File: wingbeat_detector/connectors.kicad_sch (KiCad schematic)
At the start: 2 parts, among them J1 USB_C_10137062-00021LF, J2 CONN_UMC_JACK_SMD

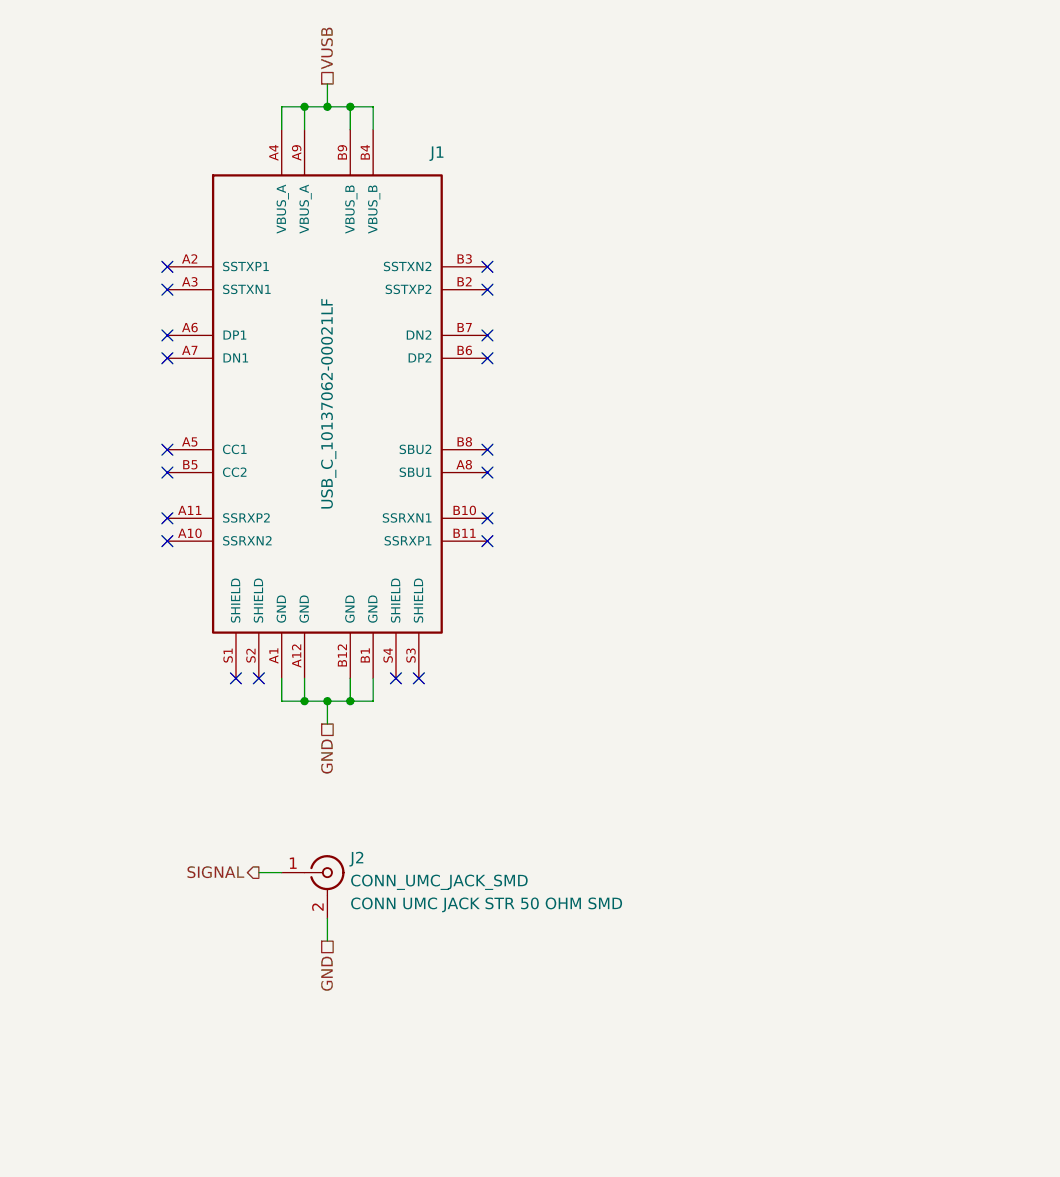
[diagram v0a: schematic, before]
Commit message: Add led driver
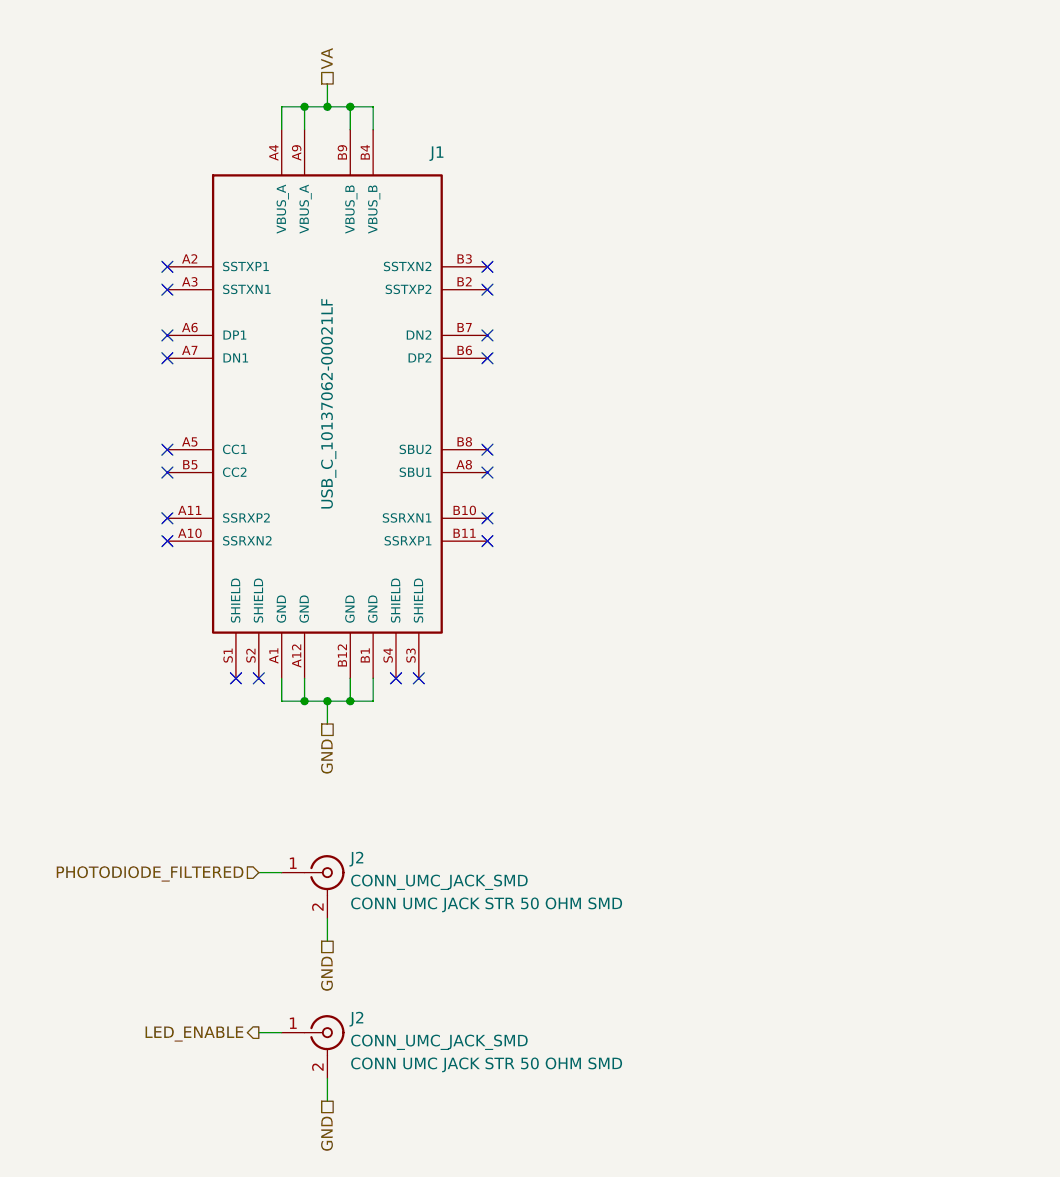
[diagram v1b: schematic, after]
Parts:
- added J2: CONN_UMC_JACK_SMD, Janelia:UMC_AMPHENOL_A-1JB, symbol Janelia:CONN_UMC_JACK_SMD
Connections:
- net GND: now also J2.2 (Ext)
- net SIGNAL renamed PHOTODIODE_FILTERED
- net VUSB renamed VA
- new net LED_ENABLE: J2.1 (In)
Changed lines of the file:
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@@
+    (stroke (width 0) (type default))
+  )
+  (wire (pts (xy 156.21 147.32) (xy 158.75 147.32))
     (stroke (width 0) (type default))
   )
@@
     (stroke (width 0) (type default))
   )
+  (wire (pts (xy 163.83 152.4) (xy 163.83 154.94))
+    (stroke (width 0) (type default))
+  )
   (wire (pts (xy 161.29 44.45) (xy 161.29 46.99))
     (stroke (width 0) (type default))
   )
-  (hierarchical_label "VUSB" (shape passive) (at 163.83 41.91 90) (fields_autoplaced)
+  (hierarchical_label "VA" (shape passive) (at 163.83 41.91 90) (fields_autoplaced)
     (effects (font (size 1.27 1.27)) (justify left))
   )
@@
     (effects (font (size 1.27 1.27)) (justify right))
   )
-  (hierarchical_label "SIGNAL" (shape output) (at 156.21 129.54 180) (fields_autoplaced)
+  (hierarchical_label "PHOTODIODE_FILTERED" (shape input) (at 156.21 129.54 180) (fields_autoplaced)
     (effects (font (size 1.27 1.27)) (justify right))
   )
+  (hierarchical_label "GND" (shape passive) (at 163.83 154.94 270) (fields_autoplaced)
+    (effects (font (size 1.27 1.27)) (justify right))
+  )
+  (hierarchical_label "LED_ENABLE" (shape output) (at 156.21 147.32 180) (fields_autoplaced)
+    (effects (font (size 1.27 1.27)) (justify right))
+  )
+  (symbol (lib_id "Janelia:CONN_UMC_JACK_SMD") (at 163.83 147.32 0) (unit 1)
+    (in_bom yes) (on_board yes) (dnp no) (fields_autoplaced)
+    (property "Reference" "J2" (at 166.37 145.7082 0)
+      (effects (font (size 1.27 1.27)) (justify left))
+    )
+    (property "Value" "CONN_UMC_JACK_SMD" (at 166.37 148.2482 0)
+      (effects (font (size 1.27 1.27)) (justify left))
+    )
+    (property "Footprint" "Janelia:UMC_AMPHENOL_A-1JB" (at 163.83 147.32 0)
+      (effects (font (size 1.27 1.27)) hide)
+    )
+    (property "Datasheet" "" (at 163.83 147.32 0)
+      (effects (font (size 1.27 1.27)) hide)
+    )
+    (property "Manufacturer" "Amphenol RF" (at 163.83 147.32 0)
+      (effects (font (size 1.27 1.27)) hide)
+    )
+    (property "Manufacturer Part Number" "A-1JB" (at 163.83 147.32 0)
+      (effects (font (size 1.27 1.27)) hide)
+    )
+    (property "Vendor" "Digi-Key" (at 163.83 147.32 0)
+      (effects (font (size 1.27 1.27)) hide)
+    )
+    (property "Vendor Part Number" "115-A-1JBCT-ND" (at 163.83 147.32 0)
+      (effects (font (size 1.27 1.27)) hide)
+    )
+    (property "Description" "CONN UMC JACK STR 50 OHM SMD" (at 166.37 150.7882 0)
+      (effects (font (size 1.27 1.27)) (justify left))
+    )
+    (pin "1")
+    (pin "2")
+    (instances
+      (project "wingbeat_detector"
+        (path "/cc457ebc-4af6-4663-b19f-8cb38f061cb4"
+          (reference "J2") (unit 1)
+        )
+        (path "/cc457ebc-4af6-4663-b19f-8cb38f061cb4/6cde90e6-6156-42e3-aaac-c45ad2bfab8b"
+          (reference "J2") (unit 1)
+        )
+        (path "/cc457ebc-4af6-4663-b19f-8cb38f061cb4/f56db15f-9297-4fc0-bdbb-85a25a2944ba"
+          (reference "J3") (unit 1)
+        )
+      )
+    )
+  )
   (symbol (lib_id "Janelia:CONN_UMC_JACK_SMD") (at 163.83 129.54 0) (unit 1)

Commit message: Add mosfet and opa381
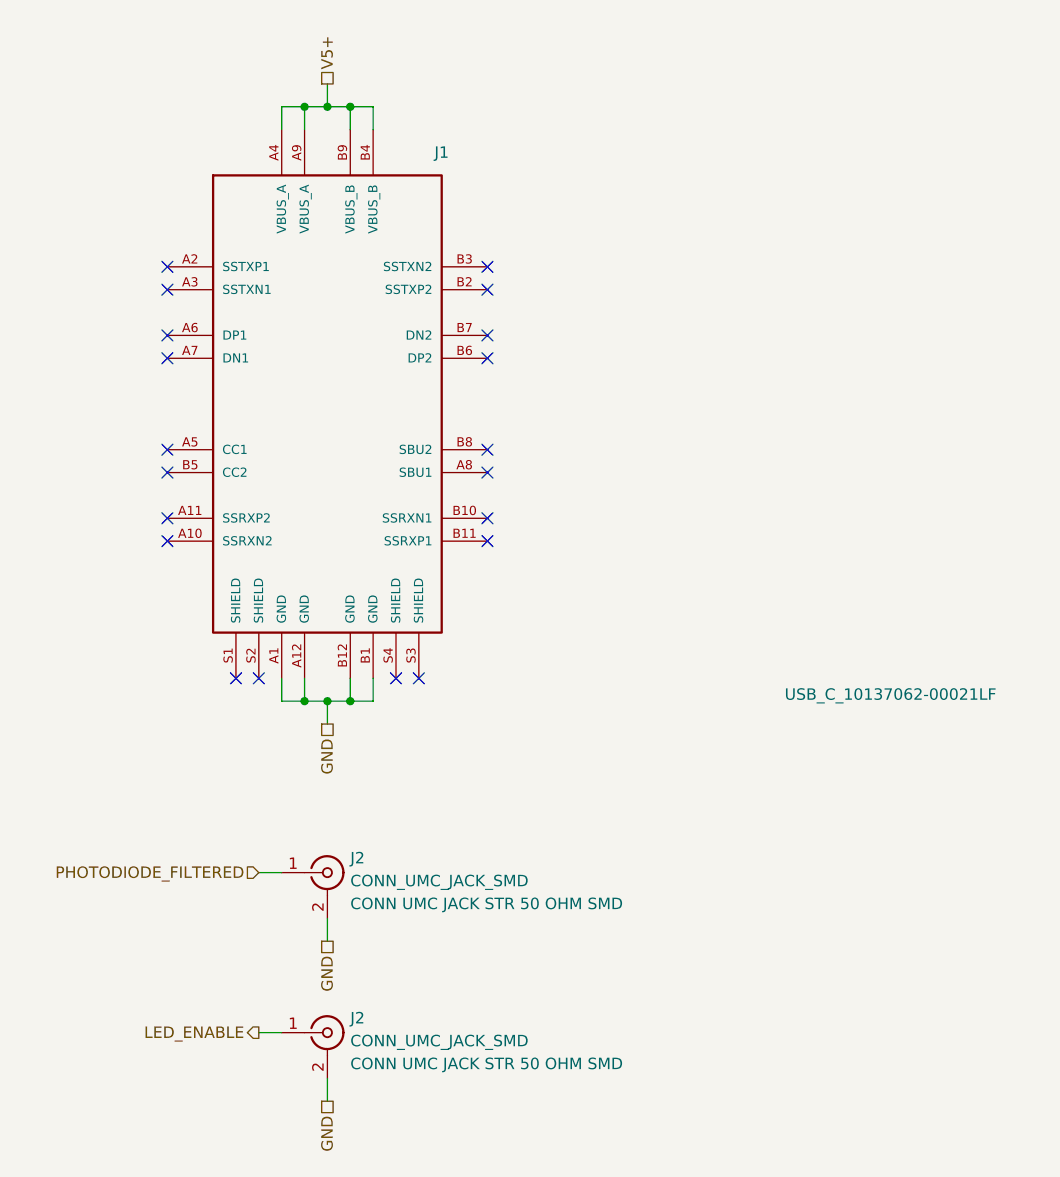
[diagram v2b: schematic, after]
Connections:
- net VA renamed V5+
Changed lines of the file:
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@@
     (stroke (width 0) (type default))
   )
-  (hierarchical_label "VA" (shape passive) (at 163.83 41.91 90) (fields_autoplaced)
+  (hierarchical_label "V5+" (shape passive) (at 163.83 41.91 90) (fields_autoplaced)
     (effects (font (size 1.27 1.27)) (justify left))
   )
@@
         )
         (path "/cc457ebc-4af6-4663-b19f-8cb38f061cb4/f56db15f-9297-4fc0-bdbb-85a25a2944ba"
-          (reference "J3") (unit 1)
+          (reference "J?") (unit 1)
         )
       )
@@
         )
         (path "/cc457ebc-4af6-4663-b19f-8cb38f061cb4/f56db15f-9297-4fc0-bdbb-85a25a2944ba"
-          (reference "J2") (unit 1)
+          (reference "J?") (unit 1)
         )
       )
@@
   (symbol (lib_id "Janelia:USB_C_10137062-00021LF") (at 163.83 77.47 0) (unit 1)
     (in_bom yes) (on_board yes) (dnp no)
-    (property "Reference" "J1" (at 175.26 49.53 0)
-      (effects (font (size 1.27 1.27)) (justify left))
-    )
-    (property "Value" "USB_C_10137062-00021LF" (at 163.83 77.47 90)
+    (property "Reference" "J1" (at 176.53 49.53 0)
       (effects (font (size 1.27 1.27)))
     )
-    (property "Footprint" "Janelia:USB_C_Receptacle_Amphenol_10137062-00021LF" (at 163.83 77.47 0)
+    (property "Value" "USB_C_10137062-00021LF" (at 214.63 110.49 0)
+      (effects (font (size 1.27 1.27)) (justify left bottom))
+    )
+    (property "Footprint" "Janelia:USB_C_Receptacle_Amphenol_10137062-00021LF" (at 163.83 -6.35 0)
+      (effects (font (size 1.27 1.27)) hide)
+    )
+    (property "Datasheet" "" (at 100.33 72.39 0)
       (effects (font (size 1.27 1.27)) (justify left bottom) hide)
     )
-    (property "Datasheet" "" (at 163.83 77.47 0)
-      (effects (font (size 1.27 1.27)) (justify left bottom) hide)
-    )
-    (property "Manufacturer" "Amphenol" (at 163.83 77.47 0)
-      (effects (font (size 1.27 1.27)) (justify left bottom) hide)
-    )
-    (property "Manufacturer Part Number" "10137062-00021LF" (at 163.83 77.47 0)
+    (property "Manufacturer" "Amphenol" (at 163.83 -1.27 0)
       (effects (font (size 1.27 1.27)) hide)
     )
-    (property "Vendor" "Digi-Key" (at 163.83 77.47 0)
+    (property "Manufacturer Part Number" "10137062-00021LF" (at 163.83 1.27 0)
       (effects (font (size 1.27 1.27)) hide)
     )
-    (property "Vendor Part Number" "609-6109-1-ND" (at 163.83 77.47 0)
+    (property "Vendor" "Digi-Key" (at 163.83 6.35 0)
       (effects (font (size 1.27 1.27)) hide)
     )
-    (property "Description" "CONN RCP USB3.1 TYPEC 24P SMD RA" (at 163.83 77.47 0)
+    (property "Vendor Part Number" "609-6109-1-ND" (at 163.83 3.81 0)
+      (effects (font (size 1.27 1.27)) hide)
+    )
+    (property "Description" "CONN RCP USB3.1 TYPEC 24P SMD RA" (at 163.83 -3.81 0)
       (effects (font (size 1.27 1.27)) hide)
     )
@@
         )
         (path "/cc457ebc-4af6-4663-b19f-8cb38f061cb4/f56db15f-9297-4fc0-bdbb-85a25a2944ba"
-          (reference "J1") (unit 1)
+          (reference "J?") (unit 1)
         )
       )
